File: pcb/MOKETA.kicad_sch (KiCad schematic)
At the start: 140 parts, among them SW43 Reset, U1 Pro_Micro

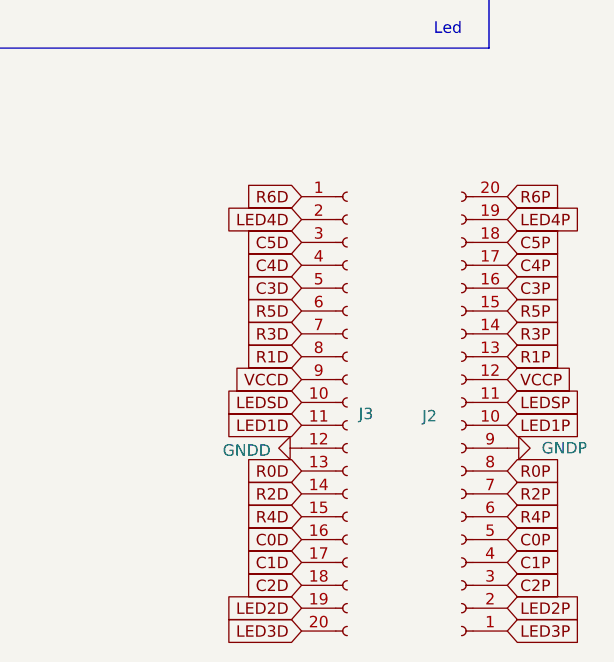
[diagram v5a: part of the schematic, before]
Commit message: Connector on doter rotated 180 degree
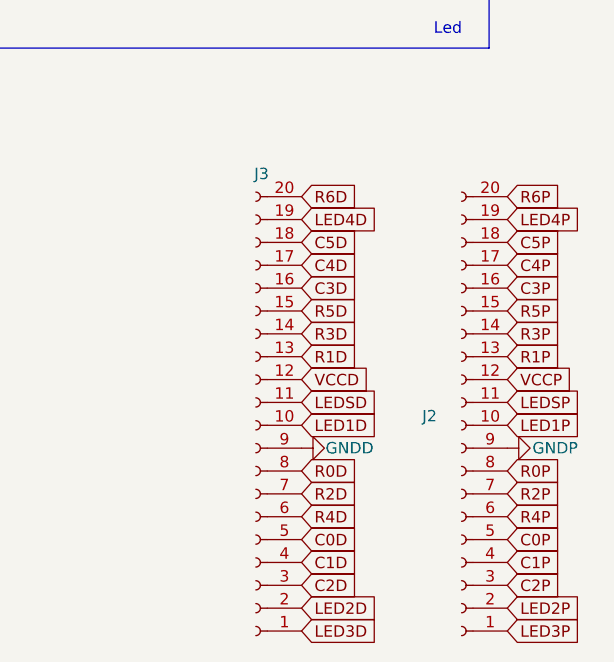
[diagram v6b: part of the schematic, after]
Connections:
- net C0D: now also J3.5 (Pin_5); no longer J3.16 (Pin_16)
- net C1D: now also J3.4 (Pin_4); no longer J3.17 (Pin_17)
- net C2D: now also J3.3 (Pin_3); no longer J3.18 (Pin_18)
- net C3D: now also J3.16 (Pin_16); no longer J3.5 (Pin_5)
- net C4D: now also J3.17 (Pin_17); no longer J3.4 (Pin_4)
- net C5D: now also J3.18 (Pin_18); no longer J3.3 (Pin_3)
- net GNDD: now also J3.9 (Pin_9); no longer J3.12 (Pin_12)
- net LED1D: now also J3.10 (Pin_10); no longer J3.11 (Pin_11)
- net LED2D: now also J3.2 (Pin_2); no longer J3.19 (Pin_19)
- net LED3D: now also J3.1 (Pin_1); no longer J3.20 (Pin_20)
- net LED4D: now also J3.19 (Pin_19); no longer J3.2 (Pin_2)
- net LEDSD: now also J3.11 (Pin_11); no longer J3.10 (Pin_10)
- net R0D: now also J3.8 (Pin_8); no longer J3.13 (Pin_13)
- net R1D: now also J3.13 (Pin_13); no longer J3.8 (Pin_8)
- net R2D: now also J3.7 (Pin_7); no longer J3.14 (Pin_14)
- net R3D: now also J3.14 (Pin_14); no longer J3.7 (Pin_7)
- net R4D: now also J3.6 (Pin_6); no longer J3.15 (Pin_15)
- net R5D: now also J3.15 (Pin_15); no longer J3.6 (Pin_6)
- net R6D: now also J3.20 (Pin_20); no longer J3.1 (Pin_1)
- net VCCD: now also J3.12 (Pin_12); no longer J3.9 (Pin_9)
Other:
- moved on the sheet: J3

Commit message: No separate doter, flex PCB instead
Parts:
- removed J2, J3: ~, moketa:FFC_CMD_1x20_P0.5mm, symbol moketa:CONN_01x20
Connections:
- net C0P is gone; now on net C0: SW1.1, SW13.1, SW19.1, SW25.1, SW31.1, SW40.1, SW7.1
- net C1P is gone; now on net C1: SW14.1, SW2.1, SW20.1, SW26.1, SW32.1, SW41.1, SW8.1
- net C2P is gone; now on net C2: SW15.1, SW21.1, SW27.1, SW3.1, SW33.1, SW42.1, SW9.1
- net C3P is gone; now on net C3: SW10.1, SW16.1, SW22.1, SW28.1, SW34.1, SW37.1, SW4.1
- net C4P is gone; now on net C4: SW11.1, SW17.1, SW23.1, SW29.1, SW35.1, SW38.1, SW5.1
- net C5P is gone; now on net C5: SW12.1, SW18.1, SW24.1, SW30.1, SW36.1, SW39.1, SW6.1
- net GNDD is gone; now on net GND: J1.2 (BAT-), U1.3 (GND), U1.4 (GND)
- net GNDP is gone; now on net GND: D43.1 (K), D44.1 (K), D45.1 (K), D46.1 (K), LED1.3 (VSS), LED10.3 (VSS), LED11.3 (VSS), LED12.3 (VSS), LED13.3 (VSS), LED14.3 (VSS), LED15.3 (VSS), LED16.3 (VSS), LED17.3 (VSS), LED18.3 (VSS), LED19.3 (VSS), LED2.3 (VSS), LED20.3 (VSS), LED21.3 (VSS), LED22.3 (VSS), LED23.3 (VSS), LED24.3 (VSS), LED25.3 (VSS), LED26.3 (VSS), LED27.3 (VSS), LED28.3 (VSS), LED29.3 (VSS), LED3.3 (VSS), LED30.3 (VSS), LED31.3 (VSS), LED32.3 (VSS), LED33.3 (VSS), LED34.3 (VSS), LED35.3 (VSS), LED36.3 (VSS), LED37.3 (VSS), LED38.3 (VSS), LED39.3 (VSS), LED4.3 (VSS), LED40.3 (VSS), LED41.3 (VSS), LED42.3 (VSS), LED5.3 (VSS), LED6.3 (VSS), LED7.3 (VSS), LED8.3 (VSS), LED9.3 (VSS)
- net LED1P is gone; now on net LED1: R1.1
- net LED2P is gone; now on net LED2: R2.1
- net LED3P is gone; now on net LED3: R3.1
- net LED4P is gone; now on net LED4: R4.1
- net LEDSP is gone; now on net LEDS: LED6.4 (DIN)
- net R0P is gone; now on net R0: D1.1 (K), D2.1 (K), D3.1 (K), D4.1 (K), D5.1 (K), D6.1 (K)
- net R1P is gone; now on net R1: D10.1 (K), D11.1 (K), D12.1 (K), D7.1 (K), D8.1 (K), D9.1 (K)
- net R2P is gone; now on net R2: D13.1 (K), D14.1 (K), D15.1 (K), D16.1 (K), D17.1 (K), D18.1 (K)
- net R3P is gone; now on net R3: D19.1 (K), D20.1 (K), D21.1 (K), D22.1 (K), D23.1 (K), D24.1 (K)
- net R4P is gone; now on net R4: D25.1 (K), D26.1 (K), D27.1 (K), D28.1 (K), D29.1 (K), D30.1 (K)
- net R5P is gone; now on net R5: D31.1 (K), D32.1 (K), D33.1 (K), D34.1 (K), D35.1 (K), D36.1 (K)
- net R6P is gone; now on net R6: D37.1 (K), D38.1 (K), D39.1 (K), D40.1 (K), D41.1 (K), D42.1 (K)
- net VCCP is gone; now on net VCC: LED1.1 (VDD), LED10.1 (VDD), LED11.1 (VDD), LED12.1 (VDD), LED13.1 (VDD), LED14.1 (VDD), LED15.1 (VDD), LED16.1 (VDD), LED17.1 (VDD), LED18.1 (VDD), LED19.1 (VDD), LED2.1 (VDD), LED20.1 (VDD), LED21.1 (VDD), LED22.1 (VDD), LED23.1 (VDD), LED24.1 (VDD), LED25.1 (VDD), LED26.1 (VDD), LED27.1 (VDD), LED28.1 (VDD), LED29.1 (VDD), LED3.1 (VDD), LED30.1 (VDD), LED31.1 (VDD), LED32.1 (VDD), LED33.1 (VDD), LED34.1 (VDD), LED35.1 (VDD), LED36.1 (VDD), LED37.1 (VDD), LED38.1 (VDD), LED39.1 (VDD), LED4.1 (VDD), LED40.1 (VDD), LED41.1 (VDD), LED42.1 (VDD), LED5.1 (VDD), LED6.1 (VDD), LED7.1 (VDD), LED8.1 (VDD), LED9.1 (VDD)
- net C0D renamed C0
- net C1D renamed C1
- net C2D renamed C2
- net C3D renamed C3
- net C4D renamed C4
- net C5D renamed C5
- net LED1D renamed LED1
- net LED2D renamed LED2
- net LED3D renamed LED3
- net LED4D renamed LED4
- net LEDSD renamed LEDS
- net R0D renamed R0
- net R1D renamed R1
- net R2D renamed R2
- net R3D renamed R3
- net R4D renamed R4
- net R5D renamed R5
- net R6D renamed R6
- net VCCD renamed VCC
